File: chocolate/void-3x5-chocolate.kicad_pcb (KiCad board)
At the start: 2 copper layers, 140.5 x 112.5 mm, 81 parts, among them J1 Conn_01x02, J2 Conn_01x03_MountingPin, J3 Conn_01x02

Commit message: choc
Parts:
- MCU1: footprint TB2086_MISC:ProMicro-dn-rev-unrouted -> TB2086_MISC:ProMicro-dn-flipped-rev-unrouted
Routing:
- net VCC: track 0.00 -> 621.6 mm, vias 0 -> 5
- net col_pinky: track 0.00 -> 241.5 mm, vias 0 -> 2
- net col_middle: track 0.00 -> 226.5 mm
- net col_ring: track 0.00 -> 203.8 mm
- net col_index: track 0.00 -> 201.3 mm, vias 0 -> 2
- net row_top: track 0.00 -> 181.0 mm
- net col_inner: track 0.00 -> 164.6 mm
- net row_home: track 0.00 -> 151.7 mm
- net row_bottom: track 0.00 -> 143.7 mm
- net row_thumb: track 0.00 -> 110.1 mm, vias 0 -> 1
- net LED_PER_KEY: track 0.00 -> 82.3 mm, vias 0 -> 3
- net Net-(L23-DOUT): track 0.00 -> 57.8 mm
- net Net-(L20-DOUT): track 0.00 -> 55.6 mm
- net Net-(L13-DIN): track 0.00 -> 54.7 mm, vias 0 -> 2
- net Net-(L10-DOUT): track 0.00 -> 54.4 mm
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
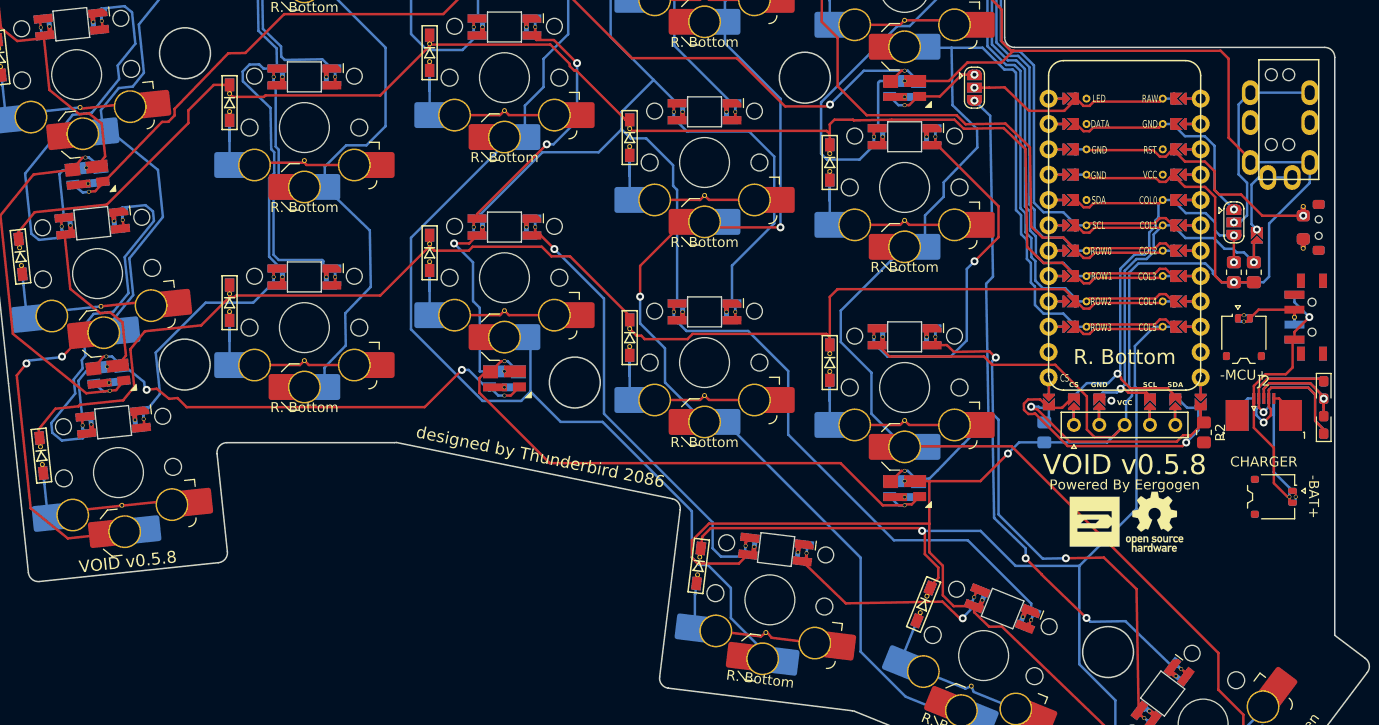
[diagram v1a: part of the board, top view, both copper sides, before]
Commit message: Choc (#4)
* updated mcu footprint for choc

* added holes for oled window

* hybrid top plate

* added hybrid top plate
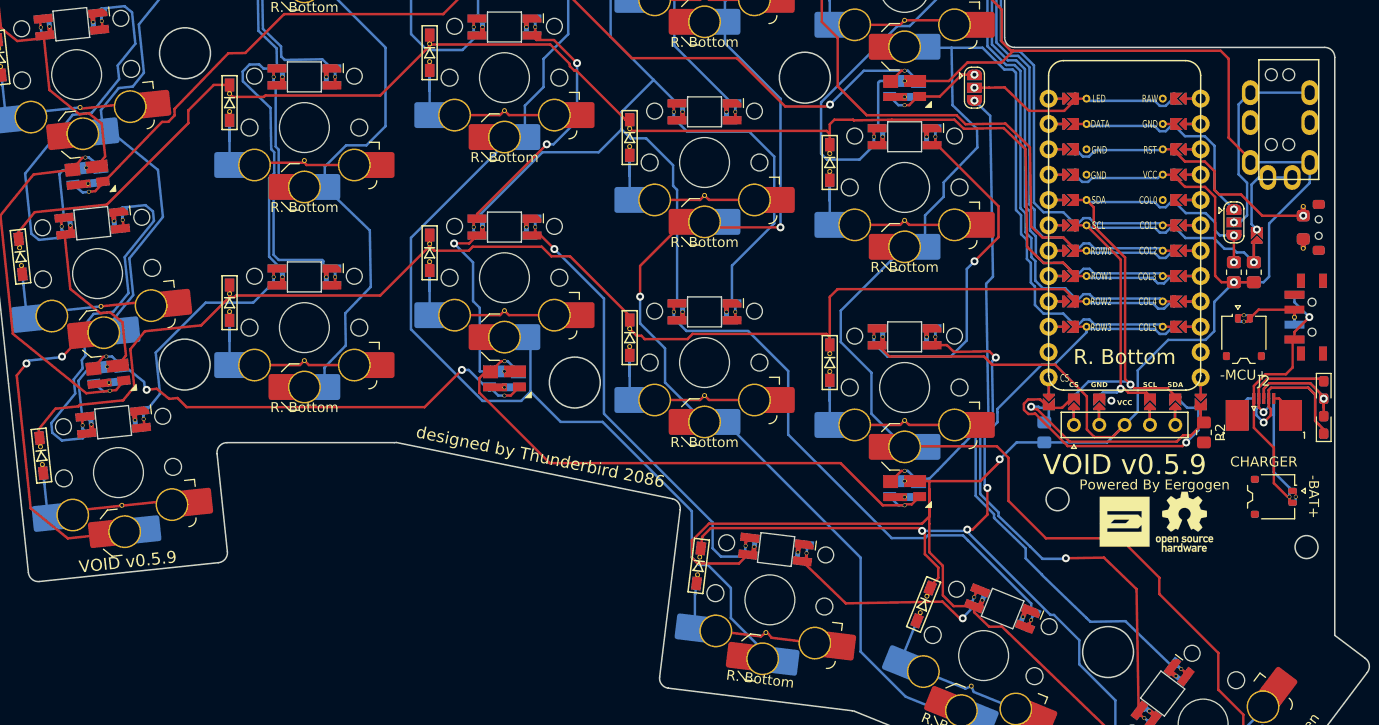
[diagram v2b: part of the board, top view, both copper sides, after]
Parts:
- MCU1: footprint TB2086_MISC:ProMicro-dn-flipped-rev-unrouted -> TB2086_MISC:ProMicro-dn-rev-unrouted
- moved LOGO1 3.00 mm to (198.7, 110.0)
- moved LOGO2 3.00 mm to (204.7, 110.0)
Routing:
- net row_thumb: track 110.1 -> 104.5 mm, vias 1 -> 3
- net col_inner: track 164.6 -> 168.1 mm
- net VCC: track 621.6 -> 618.5 mm
- net Net-(L13-DIN): track 54.7 -> 55.9 mm
- net LED_PER_KEY: track 82.3 -> 83.4 mm, vias 3 -> 1
- net GND: track 4.25 -> 5.26 mm
- net SCL: track 49.1 -> 48.2 mm
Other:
- outline, holes or cut-outs redrawn
- board text added: "VOID v0.5.9"
- board text removed: "VOID v0.5.8"

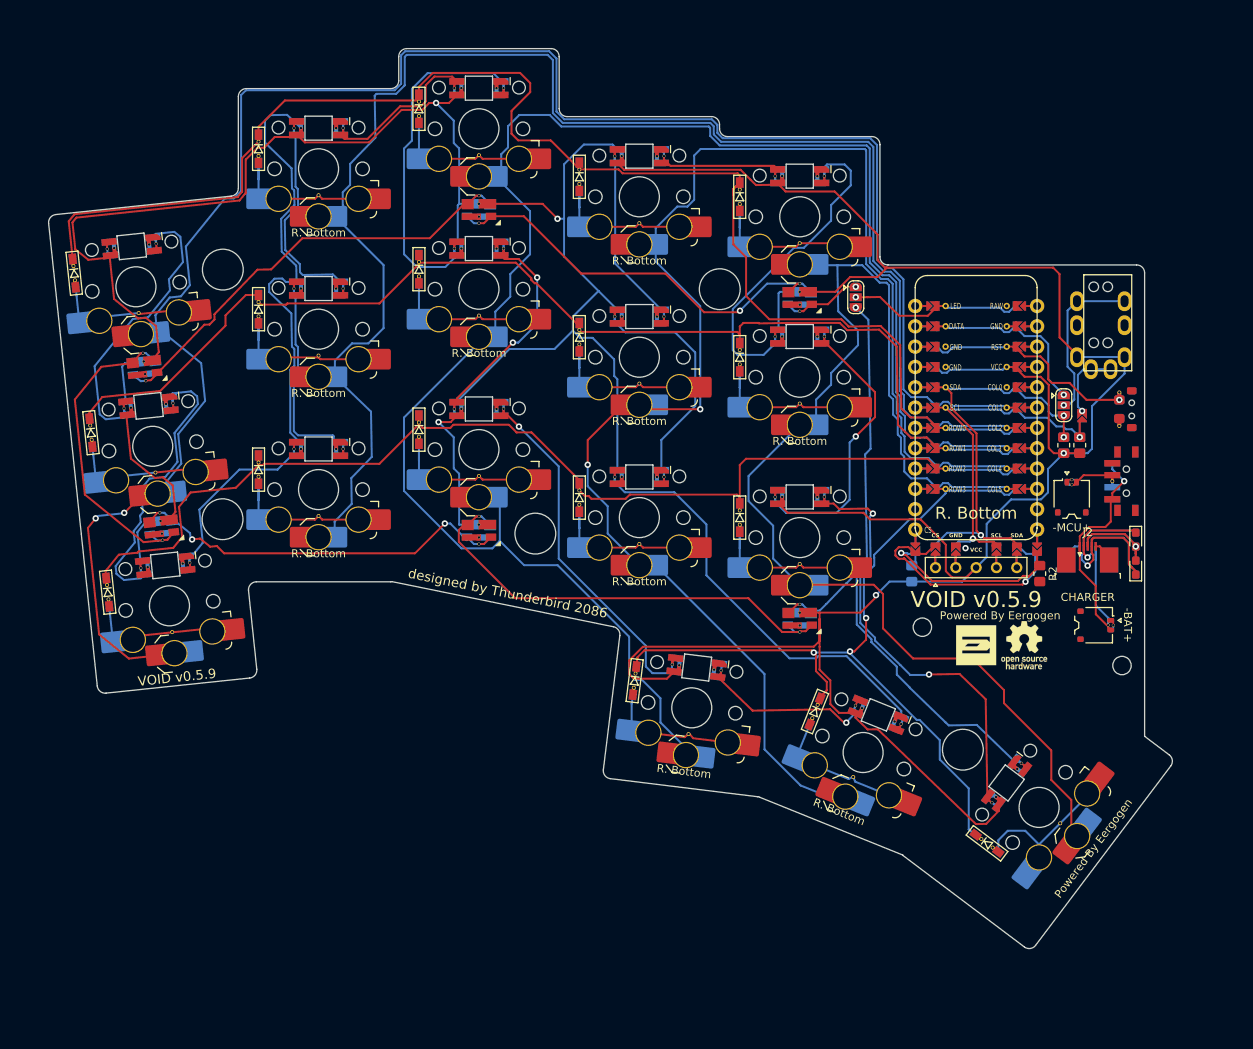
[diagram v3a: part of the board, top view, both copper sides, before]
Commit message: Changed TRRS to USB-C connector (#14)
* usb-c mod for hybrid

* updated
  - submodule
  - ergogen yaml
  - schematic and pcb

* updated cherry-mx

usb-c for communication between left and right hand sides

* updated choc

* updated choc

* fixed corner

* void-choc

* ergogen
  - bottom plate
  - charger plate

* updated choc

* updated ergogen

* cherry-mx
* hybrid-mx

* updated ergogen for VOID Choc

* refreshed submodule

* updated ergogen yaml

* updated PCBs

* updated version
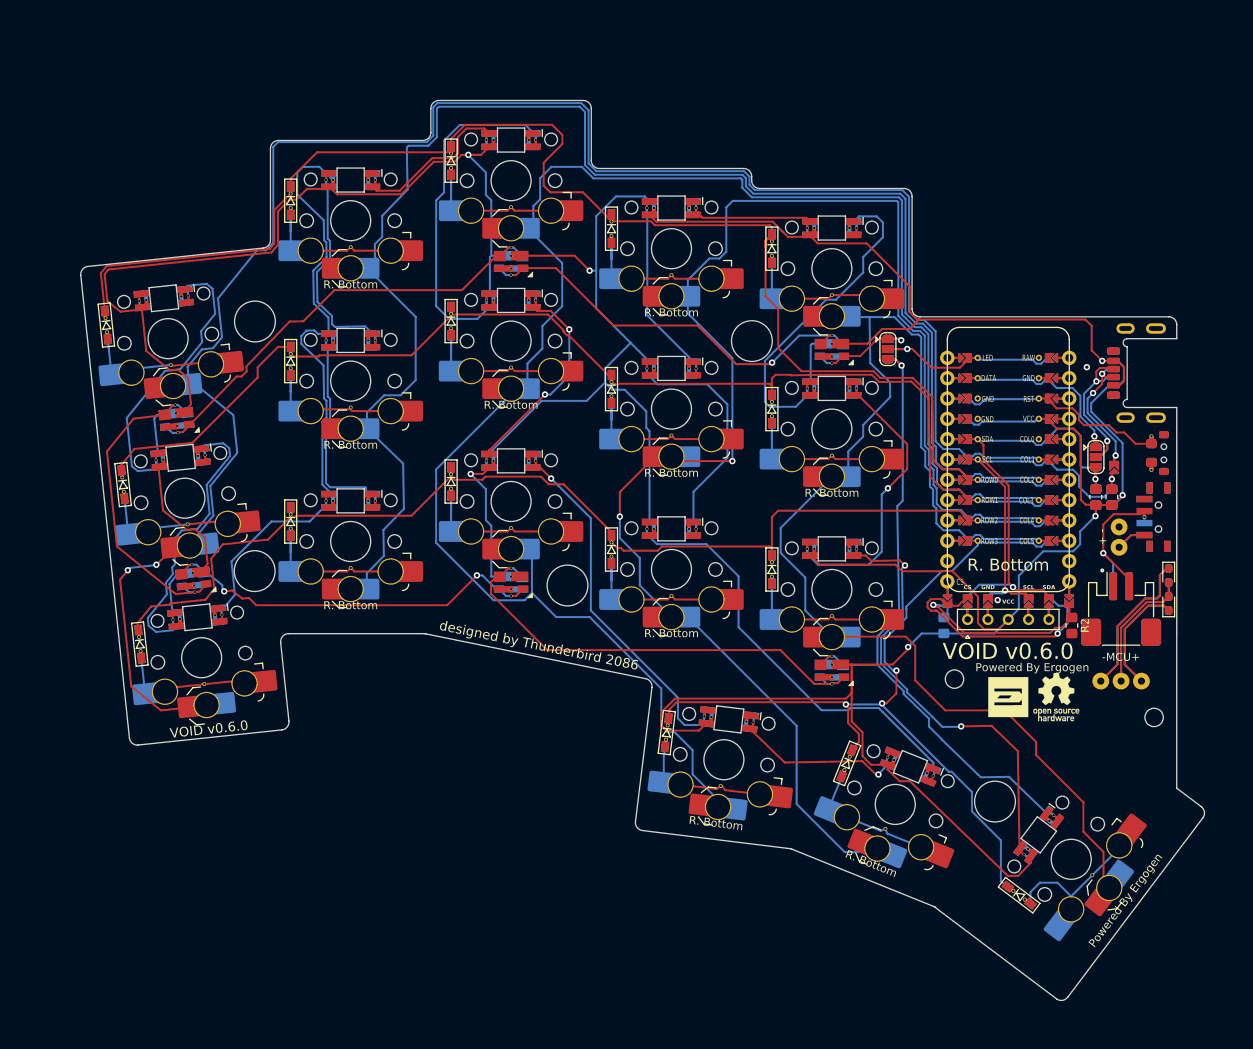
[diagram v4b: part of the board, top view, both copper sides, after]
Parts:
- removed TRRS1: MJ-4PP-9, TB2086_MISC:TRRS-PJ-320A-rev
- added J4: Conn_01x03, TB2086_MISC:Pogopin_1x03_P2.54mm, F.Cu at (216.8, 114.5)
- added SW_SPDT2: SW_SPDT2, TB2086_SMD:SW_SPDT_PCM12, F.Cu at (221.2, 94.0)
- J1: value Conn_01x02 -> USB_C_Receptacle_PowerOnly_6P; footprint TB2086_SMD:Molex_Pico-EZmate_78171-0002_1x02-1MP_P1.20mm_Vertical_rev -> TB2086_SMD:USB-20C-F-6C16_rev
- J2: value Conn_01x03_MountingPin -> Conn_01x02; footprint TB2086_SMD:TE_0-1734839-5_1x05-1MP_P0.5mm_Horizontal_rev -> TB2086_SMD:JST_PH_S2B-PH-SM4-TB_1x02-1MP_P2.00mm_Horizontal_rev
- J3: footprint TB2086_SMD:Molex_Pico-EZmate_78171-0002_1x02-1MP_P1.20mm_Vertical_rev -> TB2086_MISC:Pogopin_1x02_P2.54mm
- LED2, LED3: moved to F.Cu
- SW_SPDT1: value SW_SPDT -> SW_SPDT1; footprint TB2086_SMD:SW_SPDT_PCM12_reversible -> TB2086_SMD:SW_SPDT_PCM12
- moved J1 18.3 mm to (220.4, 76.0), turned to 90 degrees
- moved J3 11.4 mm to (216.6, 96.5)
- moved LED4 8.99 mm to (222.8, 104.8)
- moved J2 7.71 mm to (216.8, 105.5)
- moved L3 7.63 mm to (97.2, 66.7)
- moved S1 7.63 mm to (101.9, 111.6)
- moved L16 7.63 mm to (167.8, 119.3)
- moved D18 7.63 mm to (204.1, 141.3)
- moved S3 7.63 mm to (97.7, 71.7)
- moved D2 7.63 mm to (92.1, 89.9)
- moved L2 7.63 mm to (99.3, 86.6)
- moved D11 7.63 mm to (153.1, 78.0)
- moved L24 7.63 mm to (180.7, 113.1)
- moved D5 7.63 mm to (113.0, 74.5)
- moved D12 7.63 mm to (153.1, 58.0)
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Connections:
- J2 pad 1: BAT -> GND
- JP2 pad 2: Net-(JP2-C) -> Net-(J1-CC2)
- JP3 pad 2: Net-(JP3-B) -> Net-(J1-CC1)
- LED1 pad 1: Net-(J2-Pin_4) -> Net-(J4-Pin_1)
- LED1 pad 2: Net-(J2-Pin_3) -> Net-(J4-Pin_2)
- LED2 pad 1: Net-(J2-Pin_4) -> Net-(J4-Pin_1)
- LED2 pad 2: Net-(J2-Pin_3) -> Net-(J4-Pin_2)
- LED3 pad 1: Net-(J2-Pin_2) -> Net-(J4-Pin_3)
- LED3 pad 2: Net-(J2-Pin_3) -> Net-(J4-Pin_2)
- LED4 pad 1: Net-(J2-Pin_2) -> Net-(J4-Pin_3)
- LED4 pad 2: Net-(J2-Pin_3) -> Net-(J4-Pin_2)
- SW_SPDT1 pad 2: Net-(J1-Pin_2) -> Net-(J2-Pin_2)
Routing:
- net Net-(J4-Pin_1): track 0.00 -> 37.2 mm
- net Net-(J4-Pin_2): track 0.00 -> 32.0 mm
- net BAT: track 39.2 -> 7.60 mm, vias 1 -> 0
- net Net-(J4-Pin_3): track 0.00 -> 29.1 mm
- net Net-(J2-Pin_4): track 23.2 -> 0.00 mm, vias 1 -> 0
- net Net-(J1-CC2): track 0.00 -> 21.1 mm, vias 0 -> 2
- net Net-(J2-Pin_3): track 20.9 -> 0.00 mm, vias 1 -> 0
- net Net-(JP2-C): track 20.1 -> 0.00 mm, vias 1 -> 0
- net Net-(J1-CC1): track 0.00 -> 17.7 mm, vias 0 -> 3
- net Net-(JP3-B): track 9.10 -> 0.00 mm, vias 1 -> 0
- net Net-(J1-Pin_2): track 7.23 -> 0.00 mm
- net SDA: track 52.7 -> 58.3 mm, vias 3 -> 2
- net VCC: track 618.5 -> 623.9 mm, vias 5 -> 7
- net GND: track 5.26 -> 1.01 mm, vias 1 -> 2
- net LED_UNDERGLOW: track 10.1 -> 13.6 mm
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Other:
- outline, holes or cut-outs redrawn
- board text added: "- +"
- board text added: "Powered By Ergogen"
- board text added: "VOID v0.6.0"
- board text added: "offset: 90, 70 from origin"
- board text removed: "-BAT+"
- board text removed: "CHARGER"
- board text removed: "Powered By Eergogen"
- board text removed: "VOID v0.5.9"
